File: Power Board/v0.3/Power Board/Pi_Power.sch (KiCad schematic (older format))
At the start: 13 parts

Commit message: power board v0.3 - Raspberry Pi side only
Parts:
- added D1: LED, red, LED_SMD:LED_0603_1608Metric, symbol Device:LED
- added R6: 680, Resistor_SMD:R_0603_1608Metric, symbol Device:R
- C1: renamed from C?; Digikey No. (none) -> 399-6672-1-ND; Manufacturer (none) -> Kemet; Part No. (none) -> EDK107M050A9MAA
- C2: renamed from C?; footprint (none) -> Capacitor_SMD:C_1210_3225Metric
- C3, C6: renamed from C?; footprint (none) -> Capacitor_SMD:C_0805_2012Metric; Digikey No. (none) -> not avail.; Manufacturer (none) -> NIC; Part No. stock -> NMC0805X7R105K25TRPLPF
- C4: renamed from C?; footprint (none) -> Capacitor_SMD:C_0603_1608Metric; Part No. stock -> (none)
- C5: renamed from C?; footprint (none) -> Capacitor_SMD:C_0603_1608Metric; Digikey No. (none) -> 490-1517-2-ND; Manufacturer (none) -> Murata; Part No. (none) -> GRM188R71H223KA01D
- C7: renamed from C?; footprint (none) -> Capacitor_SMD:C_1210_3225Metric; Digikey No. (none) -> 587-5426-1-ND; Manufacturer (none) -> Taiyo Yuden; Part No. (none) -> EMK325ABJ107MM-P
- R1: renamed from R?; footprint (none) -> Resistor_SMD:R_0603_1608Metric; Manufacturer (none) -> Yageo; Part No. stock -> RC0603JR-0768K
- R2: renamed from R?; footprint (none) -> Resistor_SMD:R_0603_1608Metric; Manufacturer (none) -> Yageo; Part No. stock -> RC0603JR-076K8
- R3: renamed from R?; footprint (none) -> Resistor_SMD:R_0603_1608Metric; Manufacturer (none) -> Yageo; Part No. stock -> RC0603JR-07120K
- R4: renamed from R?; value 8.2K -> 5.90K 1%; footprint (none) -> Resistor_SMD:R_0603_1608Metric; Digikey No. (none) -> P5.90KHCT-ND; Manufacturer (none) -> Panasonic; Part No. stock -> ERJ-3EKF5901V
- R5: renamed from R?; value 1.5K -> 1.07K 1%; footprint (none) -> Resistor_SMD:R_0603_1608Metric; Digikey No. (none) -> P1.07KHCT-ND; Manufacturer (none) -> Panasonic; Part No. stock -> ERJ-3EKF1071V
- gave numbers to parts that had none: 1
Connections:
- net 5.1V_unswitched: now also D1.2 (A)
- net GND: now also R6.2
- new net: D1.1 (K), R6.1
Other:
- moved on the sheet: C1, C2, C3, C4, C5, C6, C7, R1, R2, R3, R4, R5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

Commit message: Revised soft power switch.  Now switches power to 5V regulator.
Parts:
- renumbered C7 to C10, C1 to C4, C2 to C5, C3 to C6, C4 to C7, C5 to C8, C6 to C9, D1 to D3, R4 to R10, R5 to R11, R6 to R12, R1 to R7, R2 to R8, R3 to R9
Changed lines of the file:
@@
 $Descr A4 11693 8268
 encoding utf-8
-Sheet 2 4
+Sheet 3 4
 Title ""
 Date ""
@@
 P 5850 3550
 AR Path="/5C94DD76" Ref="U?"  Part="1"
-AR Path="/5C93509D/5C94DD76" Ref="U1"  Part="1"
+AR Path="/5C93509D/5C94DD76" Ref="U?"  Part="1"
+AR Path="/5C958DBD/5C9BDDC9/5C94DD76" Ref="U1"  Part="1"
 F 0 "U1" H 5850 4115 50  0000 C CNN
 F 1 "LMZ14203" H 5850 4024 50  0000 C CNN
@@
 P 3050 4550
 AR Path="/5C94DD82" Ref="#PWR?"  Part="1"
-AR Path="/5C93509D/5C94DD82" Ref="#PWR04"  Part="1"
-F 0 "#PWR04" H 3050 4300 50  0001 C CNN
+AR Path="/5C93509D/5C94DD82" Ref="#PWR?"  Part="1"
+AR Path="/5C958DBD/5C9BDDC9/5C94DD82" Ref="#PWR06"  Part="1"
+F 0 "#PWR06" H 3050 4300 50  0001 C CNN
 F 1 "GND" H 3055 4377 50  0000 C CNN
 F 2 "" H 3050 4550 50  0001 C CNN
@@
 P 3450 4550
 AR Path="/5C94DD88" Ref="#PWR?"  Part="1"
-AR Path="/5C93509D/5C94DD88" Ref="#PWR05"  Part="1"
-F 0 "#PWR05" H 3450 4300 50  0001 C CNN
+AR Path="/5C93509D/5C94DD88" Ref="#PWR?"  Part="1"
+AR Path="/5C958DBD/5C9BDDC9/5C94DD88" Ref="#PWR07"  Part="1"
+F 0 "#PWR07" H 3450 4300 50  0001 C CNN
 F 1 "GND" H 3455 4377 50  0000 C CNN
 F 2 "" H 3450 4550 50  0001 C CNN
@@
 P 3850 4550
 AR Path="/5C94DD8E" Ref="#PWR?"  Part="1"
-AR Path="/5C93509D/5C94DD8E" Ref="#PWR06"  Part="1"
-F 0 "#PWR06" H 3850 4300 50  0001 C CNN
+AR Path="/5C93509D/5C94DD8E" Ref="#PWR?"  Part="1"
+AR Path="/5C958DBD/5C9BDDC9/5C94DD8E" Ref="#PWR08"  Part="1"
+F 0 "#PWR08" H 3850 4300 50  0001 C CNN
 F 1 "GND" H 3855 4377 50  0000 C CNN
 F 2 "" H 3850 4550 50  0001 C CNN
@@
 P 4250 4550
 AR Path="/5C94DD94" Ref="#PWR?"  Part="1"
-AR Path="/5C93509D/5C94DD94" Ref="#PWR07"  Part="1"
-F 0 "#PWR07" H 4250 4300 50  0001 C CNN
+AR Path="/5C93509D/5C94DD94" Ref="#PWR?"  Part="1"
+AR Path="/5C958DBD/5C9BDDC9/5C94DD94" Ref="#PWR09"  Part="1"
+F 0 "#PWR09" H 4250 4300 50  0001 C CNN
 F 1 "GND" H 4255 4377 50  0000 C CNN
 F 2 "" H 4250 4550 50  0001 C CNN
@@
 P 5850 4550
 AR Path="/5C94DD9A" Ref="#PWR?"  Part="1"
-AR Path="/5C93509D/5C94DD9A" Ref="#PWR08"  Part="1"
-F 0 "#PWR08" H 5850 4300 50  0001 C CNN
+AR Path="/5C93509D/5C94DD9A" Ref="#PWR?"  Part="1"
+AR Path="/5C958DBD/5C9BDDC9/5C94DD9A" Ref="#PWR010"  Part="1"
+F 0 "#PWR010" H 5850 4300 50  0001 C CNN
 F 1 "GND" H 5855 4377 50  0000 C CNN
 F 2 "" H 5850 4550 50  0001 C CNN
@@
 P 6650 4550
 AR Path="/5C94DDA0" Ref="#PWR?"  Part="1"
-AR Path="/5C93509D/5C94DDA0" Ref="#PWR09"  Part="1"
-F 0 "#PWR09" H 6650 4300 50  0001 C CNN
+AR Path="/5C93509D/5C94DDA0" Ref="#PWR?"  Part="1"
+AR Path="/5C958DBD/5C9BDDC9/5C94DDA0" Ref="#PWR011"  Part="1"
+F 0 "#PWR011" H 6650 4300 50  0001 C CNN
 F 1 "GND" H 6655 4377 50  0000 C CNN
 F 2 "" H 6650 4550 50  0001 C CNN
@@
 P 7450 4550
 AR Path="/5C94DDA6" Ref="#PWR?"  Part="1"
-AR Path="/5C93509D/5C94DDA6" Ref="#PWR010"  Part="1"
-F 0 "#PWR010" H 7450 4300 50  0001 C CNN
+AR Path="/5C93509D/5C94DDA6" Ref="#PWR?"  Part="1"
+AR Path="/5C958DBD/5C9BDDC9/5C94DDA6" Ref="#PWR012"  Part="1"
+F 0 "#PWR012" H 7450 4300 50  0001 C CNN
 F 1 "GND" H 7455 4377 50  0000 C CNN
 F 2 "" H 7450 4550 50  0001 C CNN
@@
 P 8250 4550
 AR Path="/5C94DDAC" Ref="#PWR?"  Part="1"
-AR Path="/5C93509D/5C94DDAC" Ref="#PWR011"  Part="1"
-F 0 "#PWR011" H 8250 4300 50  0001 C CNN
+AR Path="/5C93509D/5C94DDAC" Ref="#PWR?"  Part="1"
+AR Path="/5C958DBD/5C9BDDC9/5C94DDAC" Ref="#PWR013"  Part="1"
+F 0 "#PWR013" H 8250 4300 50  0001 C CNN
 F 1 "GND" H 8255 4377 50  0000 C CNN
 F 2 "" H 8250 4550 50  0001 C CNN
@@
 P 8650 4550
 AR Path="/5C94DDB2" Ref="#PWR?"  Part="1"
-AR Path="/5C93509D/5C94DDB2" Ref="#PWR012"  Part="1"
-F 0 "#PWR012" H 8650 4300 50  0001 C CNN
+AR Path="/5C93509D/5C94DDB2" Ref="#PWR?"  Part="1"
+AR Path="/5C958DBD/5C9BDDC9/5C94DDB2" Ref="#PWR014"  Part="1"
+F 0 "#PWR014" H 8650 4300 50  0001 C CNN
 F 1 "GND" H 8655 4377 50  0000 C CNN
 F 2 "" H 8650 4550 50  0001 C CNN
@@
 P 3450 3700
 AR Path="/5C94DDB8" Ref="C?"  Part="1"
-AR Path="/5C93509D/5C94DDB8" Ref="C2"  Part="1"
-F 0 "C2" H 3500 3800 50  0000 L CNN
+AR Path="/5C93509D/5C94DDB8" Ref="C?"  Part="1"
+AR Path="/5C958DBD/5C9BDDC9/5C94DDB8" Ref="C5"  Part="1"
+F 0 "C5" H 3500 3800 50  0000 L CNN
 F 1 "10µF" H 3500 3600 50  0000 L CNN
 F 2 "Capacitor_SMD:C_1210_3225Metric" H 3488 3550 50  0001 C CNN
@@
 P 3850 3700
 AR Path="/5C94DDC0" Ref="C?"  Part="1"
-AR Path="/5C93509D/5C94DDC0" Ref="C3"  Part="1"
-F 0 "C3" H 3900 3800 50  0000 L CNN
+AR Path="/5C93509D/5C94DDC0" Ref="C?"  Part="1"
+AR Path="/5C958DBD/5C9BDDC9/5C94DDC0" Ref="C6"  Part="1"
+F 0 "C6" H 3900 3800 50  0000 L CNN
 F 1 "1µF" H 3900 3600 50  0000 L CNN
 F 2 "Capacitor_SMD:C_0805_2012Metric" H 3888 3550 50  0001 C CNN
@@
 P 6650 4200
 AR Path="/5C94DDC8" Ref="C?"  Part="1"
-AR Path="/5C93509D/5C94DDC8" Ref="C4"  Part="1"
-F 0 "C4" H 6700 4300 50  0000 L CNN
+AR Path="/5C93509D/5C94DDC8" Ref="C?"  Part="1"
+AR Path="/5C958DBD/5C9BDDC9/5C94DDC8" Ref="C7"  Part="1"
+F 0 "C7" H 6700 4300 50  0000 L CNN
 F 1 "10nF" H 6700 4100 50  0000 L CNN
 F 2 "Capacitor_SMD:C_0603_1608Metric" H 6688 4050 50  0001 C CNN
@@
 P 7850 3700
 AR Path="/5C94DDCE" Ref="C?"  Part="1"
-AR Path="/5C93509D/5C94DDCE" Ref="C5"  Part="1"
-F 0 "C5" H 7900 3800 50  0000 L CNN
+AR Path="/5C93509D/5C94DDCE" Ref="C?"  Part="1"
+AR Path="/5C958DBD/5C9BDDC9/5C94DDCE" Ref="C8"  Part="1"
+F 0 "C8" H 7900 3800 50  0000 L CNN
 F 1 "22nF" H 7900 3600 50  0000 L CNN
 F 2 "Capacitor_SMD:C_0603_1608Metric" H 7888 3550 50  0001 C CNN
@@
 P 8250 3700
 AR Path="/5C94DDD6" Ref="C?"  Part="1"
-AR Path="/5C93509D/5C94DDD6" Ref="C6"  Part="1"
-F 0 "C6" H 8300 3800 50  0000 L CNN
+AR Path="/5C93509D/5C94DDD6" Ref="C?"  Part="1"
+AR Path="/5C958DBD/5C9BDDC9/5C94DDD6" Ref="C9"  Part="1"
+F 0 "C9" H 8300 3800 50  0000 L CNN
 F 1 "1µF" H 8300 3600 50  0000 L CNN
 F 2 "Capacitor_SMD:C_0805_2012Metric" H 8288 3550 50  0001 C CNN
@@
 P 8650 3700
 AR Path="/5C94DDDC" Ref="C?"  Part="1"
-AR Path="/5C93509D/5C94DDDC" Ref="C7"  Part="1"
-F 0 "C7" H 8700 3800 50  0000 L CNN
+AR Path="/5C93509D/5C94DDDC" Ref="C?"  Part="1"
+AR Path="/5C958DBD/5C9BDDC9/5C94DDDC" Ref="C10"  Part="1"
+F 0 "C10" H 8700 3800 50  0000 L CNN
 F 1 "100µF" H 8700 3600 50  0000 L CNN
 F 2 "Capacitor_SMD:C_1210_3225Metric" H 8688 3550 50  0001 C CNN
@@
 P 3050 3700
 AR Path="/5C94DDE2" Ref="C?"  Part="1"
-AR Path="/5C93509D/5C94DDE2" Ref="C1"  Part="1"
-F 0 "C1" H 3100 3800 50  0000 L CNN
+AR Path="/5C93509D/5C94DDE2" Ref="C?"  Part="1"
+AR Path="/5C958DBD/5C9BDDC9/5C94DDE2" Ref="C4"  Part="1"
+F 0 "C4" H 3100 3800 50  0000 L CNN
 F 1 "100µF" H 3100 3600 50  0000 L CNN
 F 2 "" H 3050 3700 50  0001 C CNN
@@
 P 7450 4200
 AR Path="/5C94DDF0" Ref="R?"  Part="1"
-AR Path="/5C93509D/5C94DDF0" Ref="R5"  Part="1"
-F 0 "R5" H 7520 4246 50  0000 L CNN
+AR Path="/5C93509D/5C94DDF0" Ref="R?"  Part="1"
+AR Path="/5C958DBD/5C9BDDC9/5C94DDF0" Ref="R11"  Part="1"
+F 0 "R11" H 7520 4246 50  0000 L CNN
 F 1 "1.07K 1%" H 7520 4155 50  0000 L CNN
 F 2 "Resistor_SMD:R_0603_1608Metric" V 7380 4200 50  0001 C CNN
@@
 P 7050 3700
 AR Path="/5C94DDF8" Ref="R?"  Part="1"
-AR Path="/5C93509D/5C94DDF8" Ref="R4"  Part="1"
-F 0 "R4" H 7120 3746 50  0000 L CNN
+AR Path="/5C93509D/5C94DDF8" Ref="R?"  Part="1"
+AR Path="/5C958DBD/5C9BDDC9/5C94DDF8" Ref="R10"  Part="1"
+F 0 "R10" H 7120 3746 50  0000 L CNN
 F 1 "5.90K 1%" H 7120 3655 50  0000 L CNN
 F 2 "Resistor_SMD:R_0603_1608Metric" V 6980 3700 50  0001 C CNN
@@
 P 4250 4200
 AR Path="/5C94DE00" Ref="R?"  Part="1"
-AR Path="/5C93509D/5C94DE00" Ref="R2"  Part="1"
-F 0 "R2" H 4320 4246 50  0000 L CNN
+AR Path="/5C93509D/5C94DE00" Ref="R?"  Part="1"
+AR Path="/5C958DBD/5C9BDDC9/5C94DE00" Ref="R8"  Part="1"
+F 0 "R8" H 4320 4246 50  0000 L CNN
 F 1 "6.8K" H 4320 4155 50  0000 L CNN
 F 2 "Resistor_SMD:R_0603_1608Metric" V 4180 4200 50  0001 C CNN
@@
 P 4900 3550
 AR Path="/5C94DE08" Ref="R?"  Part="1"
-AR Path="/5C93509D/5C94DE08" Ref="R3"  Part="1"
-F 0 "R3" V 4800 3550 50  0000 C CNN
+AR Path="/5C93509D/5C94DE08" Ref="R?"  Part="1"
+AR Path="/5C958DBD/5C9BDDC9/5C94DE08" Ref="R9"  Part="1"
+F 0 "R9" V 4800 3550 50  0000 C CNN
 F 1 "120K" V 5000 3550 50  0000 C CNN
 F 2 "Resistor_SMD:R_0603_1608Metric" V 4830 3550 50  0001 C CNN
@@
 P 4250 3700
 AR Path="/5C94DE10" Ref="R?"  Part="1"
-AR Path="/5C93509D/5C94DE10" Ref="R1"  Part="1"
-F 0 "R1" H 4320 3746 50  0000 L CNN
+AR Path="/5C93509D/5C94DE10" Ref="R?"  Part="1"
+AR Path="/5C958DBD/5C9BDDC9/5C94DE10" Ref="R7"  Part="1"
+F 0 "R7" H 4320 3746 50  0000 L CNN
 F 1 "68K" H 4320 3655 50  0000 L CNN
 F 2 "Resistor_SMD:R_0603_1608Metric" V 4180 3700 50  0001 C CNN
@@
 Connection ~ 7050 3350
 $Comp
-L Device:LED D1
+L Device:LED D?
 U 1 1 5C9469BF
 P 9050 3700
-F 0 "D1" V 9089 3582 50  0000 R CNN
+AR Path="/5C93509D/5C9469BF" Ref="D?"  Part="1"
+AR Path="/5C958DBD/5C9BDDC9/5C9469BF" Ref="D3"  Part="1"
+F 0 "D3" V 9089 3582 50  0000 R CNN
 F 1 "LED, red" V 8998 3582 50  0000 R CNN
 F 2 "LED_SMD:LED_0603_1608Metric" H 9050 3700 50  0001 C CNN
@@
 $EndComp
 $Comp
-L Device:R R6
+L Device:R R?
 U 1 1 5C9489B4
 P 9050 4200
-F 0 "R6" H 9120 4246 50  0000 L CNN
+AR Path="/5C93509D/5C9489B4" Ref="R?"  Part="1"
+AR Path="/5C958DBD/5C9BDDC9/5C9489B4" Ref="R12"  Part="1"
+F 0 "R12" H 9120 4246 50  0000 L CNN
 F 1 "680" H 9120 4155 50  0000 L CNN
 F 2 "Resistor_SMD:R_0603_1608Metric" V 8980 4200 50  0001 C CNN
@@
 P 9050 4550
 AR Path="/5C948DFA" Ref="#PWR?"  Part="1"
-AR Path="/5C93509D/5C948DFA" Ref="#PWR013"  Part="1"
-F 0 "#PWR013" H 9050 4300 50  0001 C CNN
+AR Path="/5C93509D/5C948DFA" Ref="#PWR?"  Part="1"
+AR Path="/5C958DBD/5C9BDDC9/5C948DFA" Ref="#PWR015"  Part="1"
+F 0 "#PWR015" H 9050 4300 50  0001 C CNN
 F 1 "GND" H 9055 4377 50  0000 C CNN
 F 2 "" H 9050 4550 50  0001 C CNN

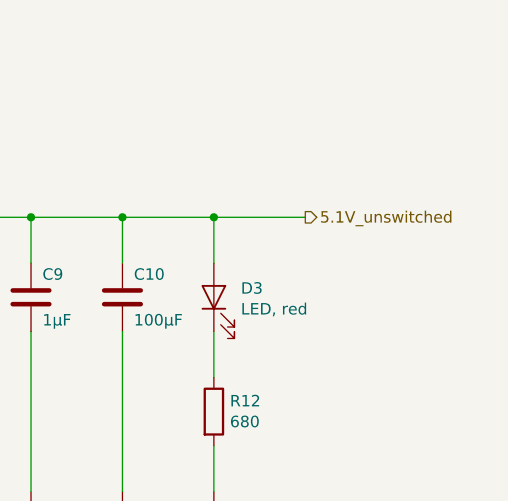
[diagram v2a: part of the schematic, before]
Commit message: Merge Pi_Power schematic into Soft_Switch.
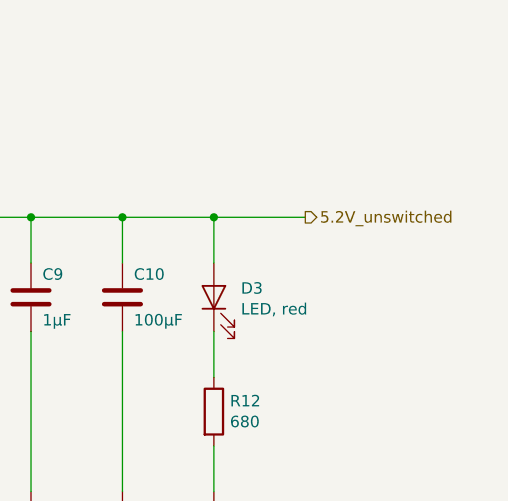
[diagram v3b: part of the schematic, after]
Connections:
- net 5.1V_unswitched renamed 5.2V_unswitched
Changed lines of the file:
@@
 $Descr A4 11693 8268
 encoding utf-8
-Sheet 3 4
+Sheet 4 4
 Title ""
 Date ""
@@
 Battery_Power
 Text HLabel 9450 3350 2    50   Output ~ 0
-5.1V_unswitched
+5.2V_unswitched
 Wire Wire Line
 	2300 3350 3050 3350
